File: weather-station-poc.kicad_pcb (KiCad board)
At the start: 4 copper layers, 165 x 91.2 mm, 136 parts, among them IC1 632723100011, IC2 TCPP01-M12, IC3 USBLC6-2SC6, IC4 BME690, IC5 S2-LPQTR, IC6 BALF-SPI2-01D3, IC7 STSAFA110S8OCD03, J1 Conn_ARM_JTAG_SWD_10, J2 61300311121, J3 61300311121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

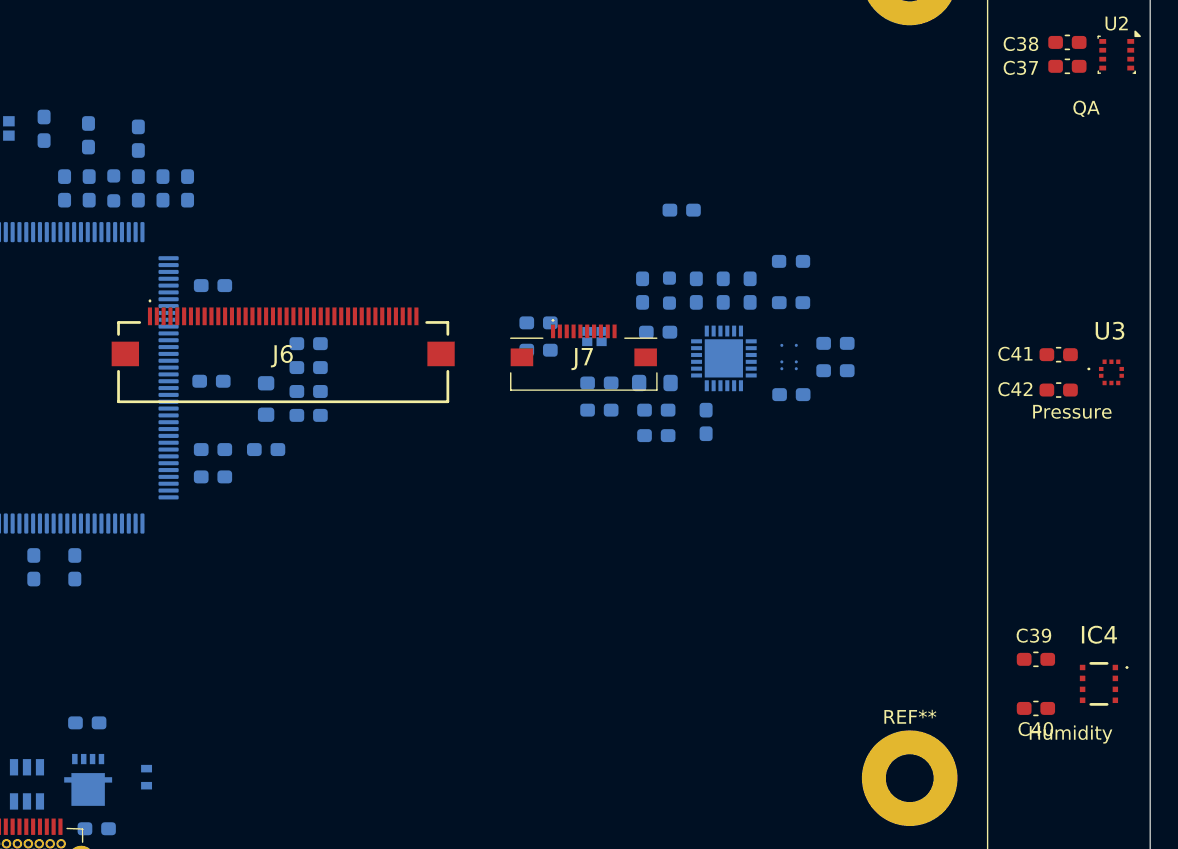
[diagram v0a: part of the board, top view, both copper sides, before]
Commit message: Bad placement of serigraphy on bottom for some components
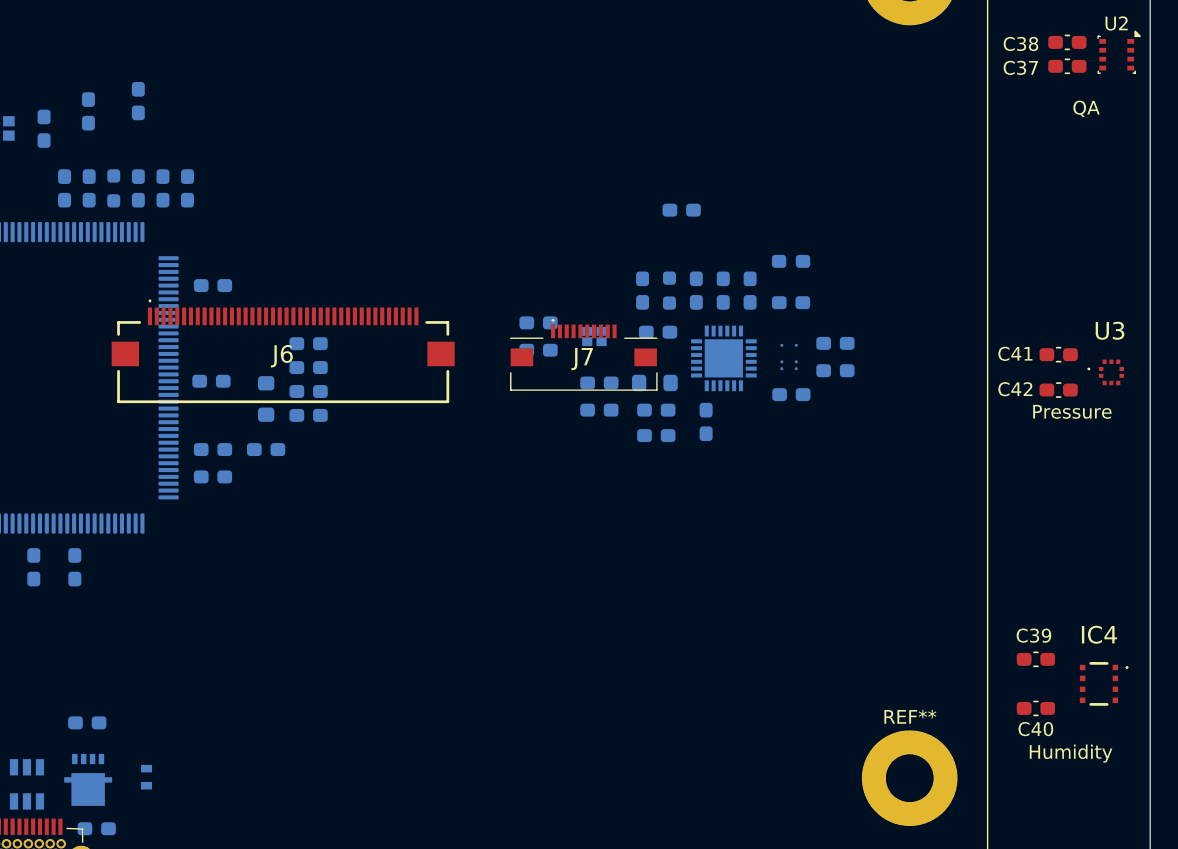
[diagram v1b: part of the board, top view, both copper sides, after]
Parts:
- moved C13 2.75 mm to (154.2, 71.2)
- moved C18 1.75 mm to (150.5, 72.0)
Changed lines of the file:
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@@
 		(tags "capacitor handsolder")
 		(property "Reference" "C11"
-			(at 3.3375 0.1 90)
+			(at 3.1375 0.1 90)
 			(layer "B.SilkS")
 			(effects
@@
 	(footprint "Capacitor_SMD:C_0603_1608Metric_Pad1.08x0.95mm_HandSolder"
 		(layer "B.Cu")
-		(at 150.5 73.75 90)
+		(at 150.5 72 90)
 		(descr "Capacitor SMD 0603 (1608 Metric), square (rectangular) end terminal, IPC-7351 nominal with elongated pad for handsoldering. (Body size source: IPC-SM-782 page 76, https://www.pcb-3d.com/wordpress/wp-content/uploads/ipc-sm-782a_amendment_1_and_2.pdf), generated with kicad-footprint-generator")
 		(tags "capacitor handsolder")
@@
 		(tags "capacitor handsolder")
 		(property "Reference" "C62"
-			(at 2.6375 -0.5 180)
+			(at 3.37692 0 90)
 			(layer "B.SilkS")
 			(effects
@@
 		(tags "capacitor handsolder")
 		(property "Reference" "C63"
-			(at 2.6375 0.5 180)
+			(at 3.37692 0.125 270)
 			(layer "B.SilkS")
 			(effects
@@
 		(tags "capacitor handsolder")
 		(property "Reference" "C60"
-			(at 2.6375 -0.5 0)
+			(at 3.24808 -0.125 90)
 			(layer "B.SilkS")
 			(effects
@@
 		(tags "capacitor handsolder")
 		(property "Reference" "C12"
-			(at 0 1.43 90)
+			(at 3.1375 0.05 90)
 			(layer "B.SilkS")
 			(effects
@@
 		(tags "capacitor handsolder")
 		(property "Reference" "C14"
-			(at -3.3375 -0.05 90)
+			(at 3.1375 -0.05 90)
 			(layer "B.SilkS")
 			(effects
@@
 		(tags "capacitor handsolder")
 		(property "Reference" "C61"
-			(at 2.7375 0.5 0)
+			(at 3.24808 0 90)
 			(layer "B.SilkS")
 			(effects
@@
 		(tags "resistor handsolder")
 		(property "Reference" "R9"
-			(at 0 1.43 90)
+			(at -2.87308 0 90)
 			(layer "B.SilkS")
 			(effects
@@
 	(footprint "Capacitor_SMD:C_0603_1608Metric_Pad1.08x0.95mm_HandSolder"
 		(layer "B.Cu")
-		(at 154.15 74 90)
+		(at 154.15 71.25 90)
 		(descr "Capacitor SMD 0603 (1608 Metric), square (rectangular) end terminal, IPC-7351 nominal with elongated pad for handsoldering. (Body size source: IPC-SM-782 page 76, https://www.pcb-3d.com/wordpress/wp-content/uploads/ipc-sm-782a_amendment_1_and_2.pdf), generated with kicad-footprint-generator")
 		(tags "capacitor handsolder")
@@
 	)
 	(gr_text "Humidity"
-		(at 219.25 118.103625 0)
+		(at 219.25 119.5 0)
 		(layer "F.SilkS")
 		(effects

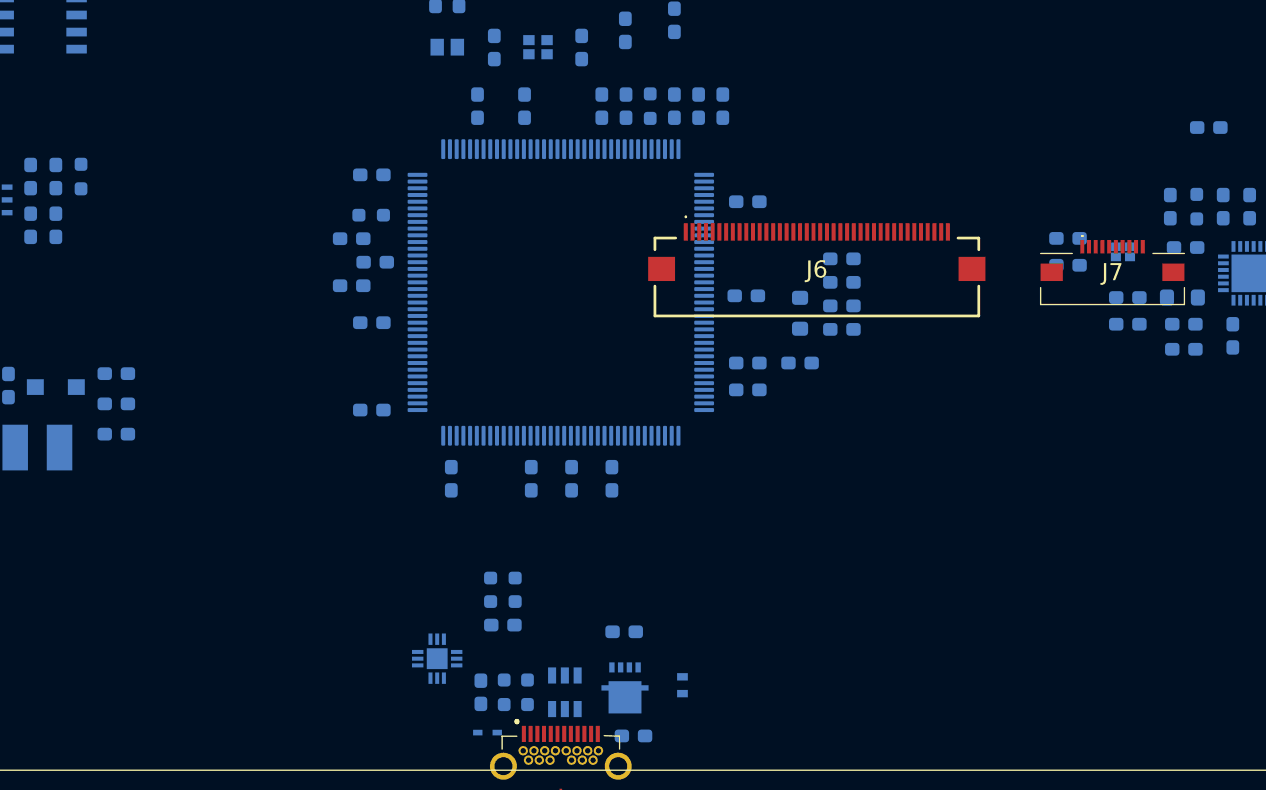
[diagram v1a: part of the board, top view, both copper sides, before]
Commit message: Place J6 and J7 FFC connector to take in account spacer height
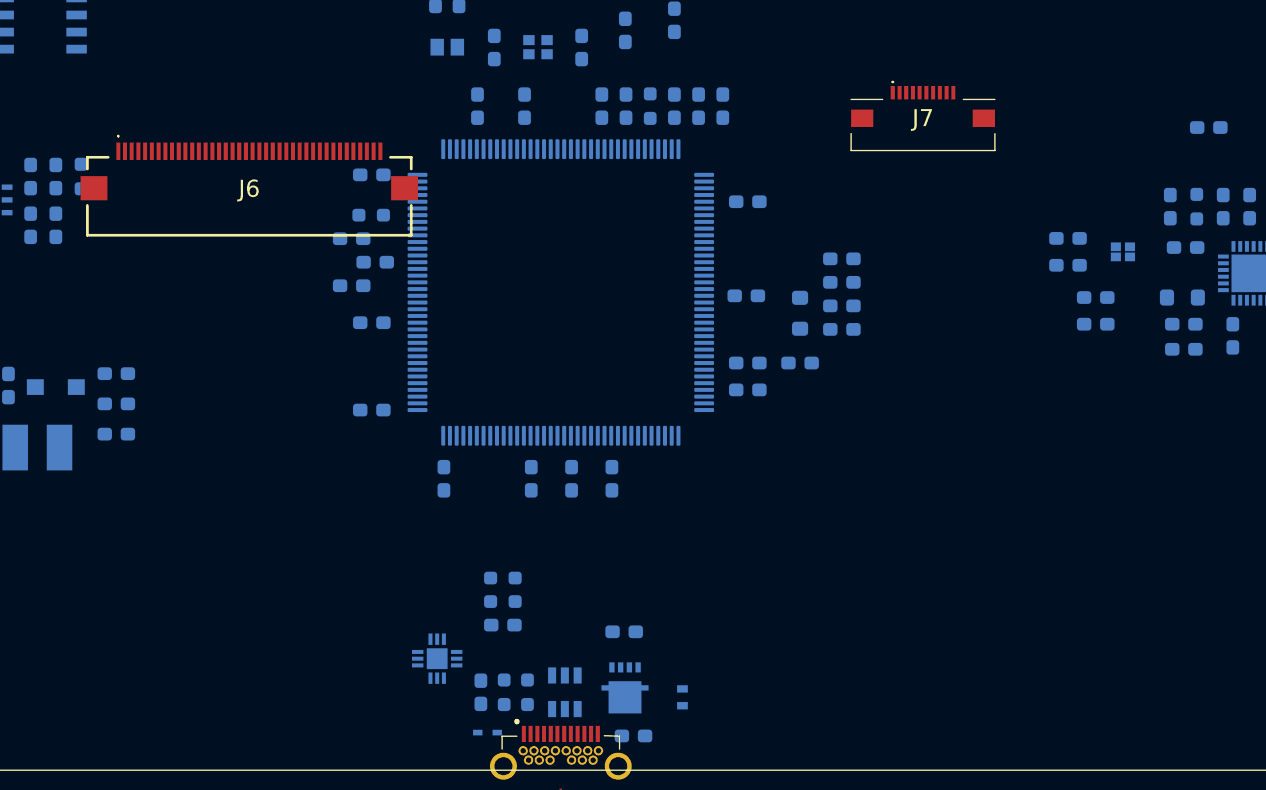
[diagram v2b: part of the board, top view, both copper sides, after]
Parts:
- moved J6 42.7 mm to (122.5, 84.1)
- moved J7 18.2 mm to (172.7, 78.5)
- moved C46 2.39 mm to (185.5, 93.9)
- moved C47 2.39 mm to (185.5, 91.9)
- moved D1 0.90 mm to (154.8, 121.6)
- moved C8 0.55 mm to (137.0, 105.4)
